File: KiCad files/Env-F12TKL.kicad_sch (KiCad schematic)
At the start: 223 parts, among them J1 TSA343G00-250J2, U1 SOT-23-5 5.5V 3.3V 500mA, U2 RP2040, Y1 3225_4P

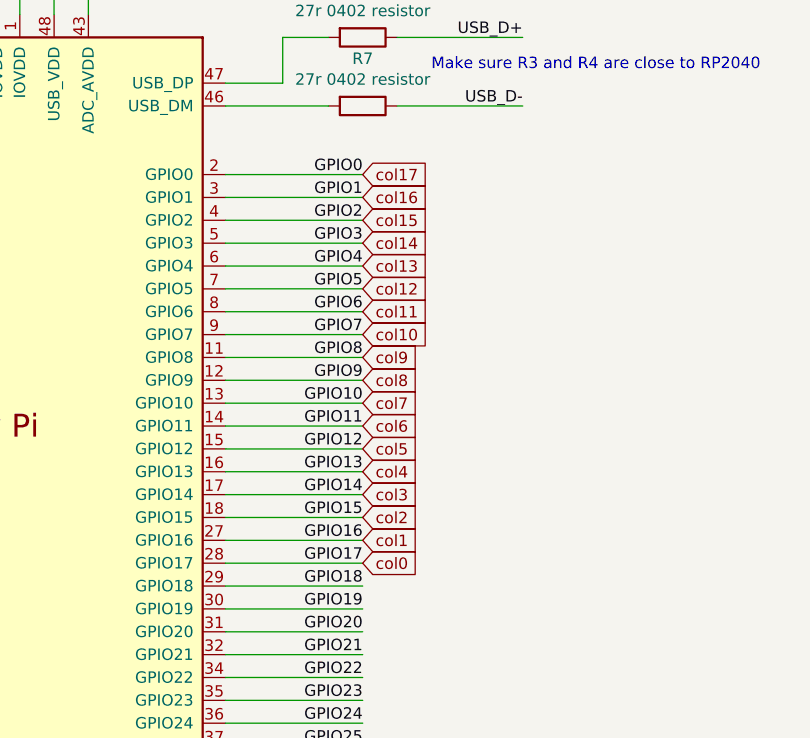
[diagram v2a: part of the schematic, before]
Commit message: undo of some work and rotated a switch due to physical incompatibility with case
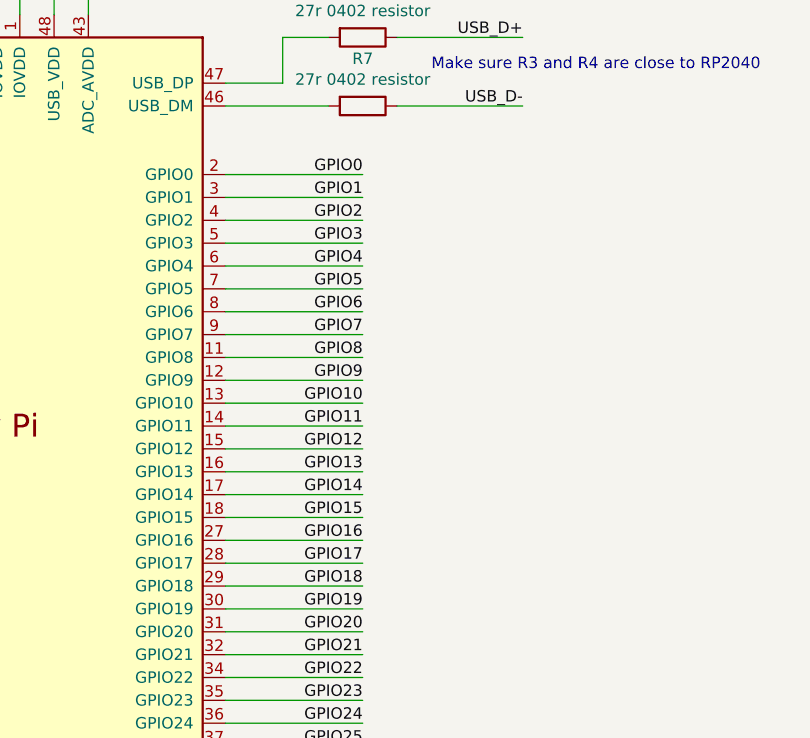
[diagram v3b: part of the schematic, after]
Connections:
- net col0: no longer U2.28 (GPIO17)
- net col1: no longer U2.27 (GPIO16)
- net col10: no longer U2.9 (GPIO7)
- net col11: no longer U2.8 (GPIO6)
- net col12: no longer U2.7 (GPIO5)
- net col13: no longer U2.6 (GPIO4)
- net col14: no longer U2.5 (GPIO3)
- net col15: no longer U2.4 (GPIO2)
- net col16: no longer U2.3 (GPIO1)
- net col17: no longer U2.2 (GPIO0)
- net col2: no longer U2.18 (GPIO15)
- net col3: no longer U2.17 (GPIO14)
- net col4: no longer U2.16 (GPIO13)
- net col5: no longer U2.15 (GPIO12)
- net col6: no longer U2.14 (GPIO11)
- net col7: no longer U2.13 (GPIO10)
- net col8: no longer U2.12 (GPIO9)
- net col9: no longer U2.11 (GPIO8)
- new net GPIO0: U2.2 (GPIO0)
- new net GPIO1: U2.3 (GPIO1)
- new net GPIO10: U2.13 (GPIO10)
- new net GPIO11: U2.14 (GPIO11)
- new net GPIO12: U2.15 (GPIO12)
- new net GPIO13: U2.16 (GPIO13)
- new net GPIO14: U2.17 (GPIO14)
- new net GPIO15: U2.18 (GPIO15)
- new net GPIO16: U2.27 (GPIO16)
- new net GPIO17: U2.28 (GPIO17)
- new net GPIO2: U2.4 (GPIO2)
- new net GPIO3: U2.5 (GPIO3)
- new net GPIO4: U2.6 (GPIO4)
- new net GPIO5: U2.7 (GPIO5)
- new net GPIO6: U2.8 (GPIO6)
- new net GPIO7: U2.9 (GPIO7)
- new net GPIO8: U2.11 (GPIO8)
- new net GPIO9: U2.12 (GPIO9)
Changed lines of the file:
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@@
     (effects (font (size 1.27 1.27)) (justify right bottom))
   )
-  (global_label "col1" (shape input) (at 299.72 340.36 0) (fields_autoplaced)
-    (effects (font (size 1.27 1.27)) (justify left))
-    (property "Intersheet References" "${INTERSHEET_REFS}" (id 0) (at 306.436 340.4394 0)
-      (effects (font (size 1.27 1.27)) (justify left) hide)
-    )
-  )
-  (global_label "col6" (shape input) (at 299.72 327.66 0) (fields_autoplaced)
-    (effects (font (size 1.27 1.27)) (justify left))
-    (property "Intersheet References" "${INTERSHEET_REFS}" (id 0) (at 306.436 327.7394 0)
-      (effects (font (size 1.27 1.27)) (justify left) hide)
-    )
-  )
   (global_label "row0" (shape input) (at 31.75 43.18 180) (fields_autoplaced)
     (effects (font (size 1.27 1.27)) (justify right))
@@
     (property "Intersheet References" "${INTERSHEET_REFS}" (id 0) (at 3.81 7.62 0)
       (effects (font (size 1.27 1.27)) hide)
-    )
-  )
-  (global_label "col13" (shape input) (at 299.72 309.88 0) (fields_autoplaced)
-    (effects (font (size 1.27 1.27)) (justify left))
-    (property "Intersheet References" "${INTERSHEET_REFS}" (id 0) (at 306.436 309.9594 0)
-      (effects (font (size 1.27 1.27)) (justify left) hide)
     )
   )
@@
     )
   )
-  (global_label "col16" (shape input) (at 299.72 302.26 0) (fields_autoplaced)
-    (effects (font (size 1.27 1.27)) (justify left))
-    (property "Intersheet References" "${INTERSHEET_REFS}" (id 0) (at 306.436 302.3394 0)
-      (effects (font (size 1.27 1.27)) (justify left) hide)
-    )
-  )
   (global_label "col14" (shape input) (at 405.13 24.13 180) (fields_autoplaced)
     (effects (font (size 1.27 1.27)) (justify right))
@@
     )
   )
-  (global_label "col12" (shape input) (at 299.72 312.42 0) (fields_autoplaced)
-    (effects (font (size 1.27 1.27)) (justify left))
-    (property "Intersheet References" "${INTERSHEET_REFS}" (id 0) (at 306.436 312.4994 0)
-      (effects (font (size 1.27 1.27)) (justify left) hide)
-    )
-  )
   (global_label "3V3_EN" (shape input) (at 63.5 269.24 270) (fields_autoplaced)
     (effects (font (size 1.27 1.27)) (justify right))
     (property "Intersheet References" "${INTERSHEET_REFS}" (id 0) (at -16.51 212.09 0)
       (effects (font (size 1.27 1.27)) hide)
-    )
-  )
-  (global_label "col10" (shape input) (at 299.72 317.5 0) (fields_autoplaced)
-    (effects (font (size 1.27 1.27)) (justify left))
-    (property "Intersheet References" "${INTERSHEET_REFS}" (id 0) (at 306.436 317.5794 0)
-      (effects (font (size 1.27 1.27)) (justify left) hide)
     )
   )
@@
     )
   )
-  (global_label "col17" (shape input) (at 299.72 299.72 0) (fields_autoplaced)
-    (effects (font (size 1.27 1.27)) (justify left))
-    (property "Intersheet References" "${INTERSHEET_REFS}" (id 0) (at 306.436 299.7994 0)
-      (effects (font (size 1.27 1.27)) (justify left) hide)
-    )
-  )
-  (global_label "col9" (shape input) (at 299.72 320.04 0) (fields_autoplaced)
-    (effects (font (size 1.27 1.27)) (justify left))
-    (property "Intersheet References" "${INTERSHEET_REFS}" (id 0) (at 306.436 320.1194 0)
-      (effects (font (size 1.27 1.27)) (justify left) hide)
-    )
-  )
   (global_label "col17" (shape input) (at 481.33 24.13 180) (fields_autoplaced)
     (effects (font (size 1.27 1.27)) (justify right))
@@
     (property "Intersheet References" "${INTERSHEET_REFS}" (id 0) (at 3.81 7.62 0)
       (effects (font (size 1.27 1.27)) hide)
-    )
-  )
-  (global_label "col7" (shape input) (at 299.72 325.12 0) (fields_autoplaced)
-    (effects (font (size 1.27 1.27)) (justify left))
-    (property "Intersheet References" "${INTERSHEET_REFS}" (id 0) (at 306.436 325.1994 0)
-      (effects (font (size 1.27 1.27)) (justify left) hide)
     )
   )
@@
     )
   )
-  (global_label "col3" (shape input) (at 299.72 335.28 0) (fields_autoplaced)
-    (effects (font (size 1.27 1.27)) (justify left))
-    (property "Intersheet References" "${INTERSHEET_REFS}" (id 0) (at 306.436 335.3594 0)
-      (effects (font (size 1.27 1.27)) (justify left) hide)
-    )
-  )
   (global_label "col1" (shape input) (at 74.93 24.13 180) (fields_autoplaced)
     (effects (font (size 1.27 1.27)) (justify right))
@@
     )
   )
-  (global_label "col8" (shape input) (at 299.72 322.58 0) (fields_autoplaced)
-    (effects (font (size 1.27 1.27)) (justify left))
-    (property "Intersheet References" "${INTERSHEET_REFS}" (id 0) (at 306.436 322.6594 0)
-      (effects (font (size 1.27 1.27)) (justify left) hide)
-    )
-  )
   (global_label "col13" (shape input) (at 379.73 24.13 180) (fields_autoplaced)
     (effects (font (size 1.27 1.27)) (justify right))
@@
     )
   )
-  (global_label "col11" (shape input) (at 299.72 314.96 0) (fields_autoplaced)
-    (effects (font (size 1.27 1.27)) (justify left))
-    (property "Intersheet References" "${INTERSHEET_REFS}" (id 0) (at 306.436 315.0394 0)
-      (effects (font (size 1.27 1.27)) (justify left) hide)
-    )
-  )
   (global_label "XOUT" (shape input) (at 219.71 340.36 180) (fields_autoplaced)
     (effects (font (size 1.27 1.27)) (justify right))
@@
     )
   )
-  (global_label "col2" (shape input) (at 299.72 337.82 0) (fields_autoplaced)
-    (effects (font (size 1.27 1.27)) (justify left))
-    (property "Intersheet References" "${INTERSHEET_REFS}" (id 0) (at 306.436 337.8994 0)
-      (effects (font (size 1.27 1.27)) (justify left) hide)
-    )
-  )
   (global_label "col16" (shape input) (at 455.93 24.13 180) (fields_autoplaced)
     (effects (font (size 1.27 1.27)) (justify right))
@@
     )
   )
-  (global_label "col5" (shape input) (at 299.72 330.2 0) (fields_autoplaced)
-    (effects (font (size 1.27 1.27)) (justify left))
-    (property "Intersheet References" "${INTERSHEET_REFS}" (id 0) (at 306.436 330.2794 0)
-      (effects (font (size 1.27 1.27)) (justify left) hide)
-    )
-  )
   (global_label "col3" (shape input) (at 125.73 24.13 180) (fields_autoplaced)
     (effects (font (size 1.27 1.27)) (justify right))
@@
     )
   )
-  (global_label "col14" (shape input) (at 299.72 307.34 0) (fields_autoplaced)
-    (effects (font (size 1.27 1.27)) (justify left))
-    (property "Intersheet References" "${INTERSHEET_REFS}" (id 0) (at 306.436 307.4194 0)
-      (effects (font (size 1.27 1.27)) (justify left) hide)
-    )
-  )
   (global_label "col0" (shape input) (at 49.53 24.13 180) (fields_autoplaced)
     (effects (font (size 1.27 1.27)) (justify right))
@@
     )
   )
-  (global_label "col4" (shape input) (at 299.72 332.74 0) (fields_autoplaced)
-    (effects (font (size 1.27 1.27)) (justify left))
-    (property "Intersheet References" "${INTERSHEET_REFS}" (id 0) (at 306.436 332.8194 0)
-      (effects (font (size 1.27 1.27)) (justify left) hide)
-    )
-  )
-  (global_label "col0" (shape input) (at 299.72 342.9 0) (fields_autoplaced)
-    (effects (font (size 1.27 1.27)) (justify left))
-    (property "Intersheet References" "${INTERSHEET_REFS}" (id 0) (at 306.436 342.9794 0)
-      (effects (font (size 1.27 1.27)) (justify left) hide)
-    )
-  )
-  (global_label "col15" (shape input) (at 299.72 304.8 0) (fields_autoplaced)
-    (effects (font (size 1.27 1.27)) (justify left))
-    (property "Intersheet References" "${INTERSHEET_REFS}" (id 0) (at 306.436 304.8794 0)
-      (effects (font (size 1.27 1.27)) (justify left) hide)
-    )
-  )
